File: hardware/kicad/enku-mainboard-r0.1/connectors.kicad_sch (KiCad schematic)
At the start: 4 parts

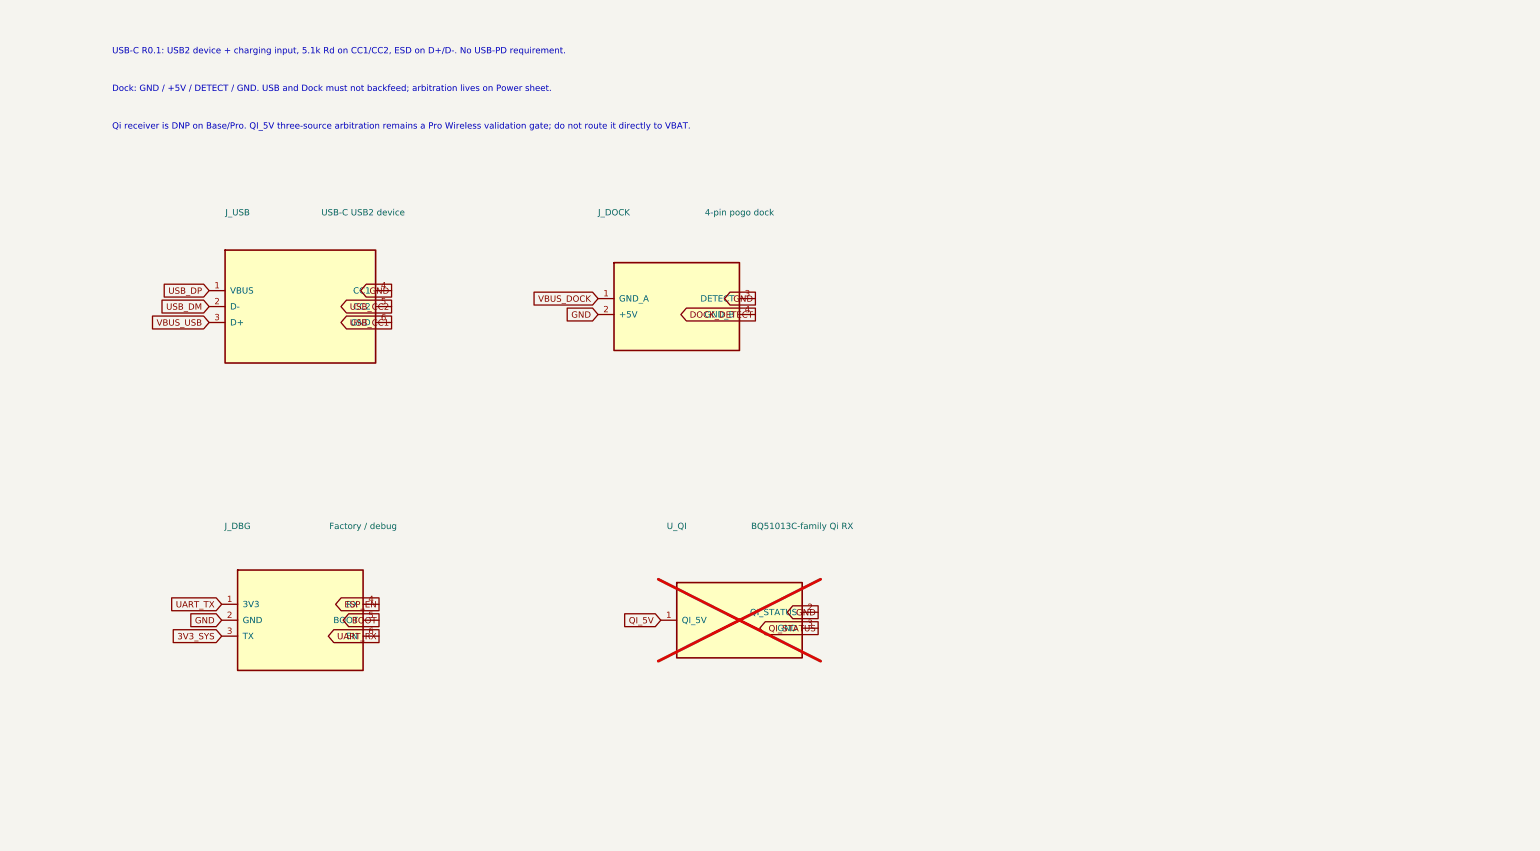
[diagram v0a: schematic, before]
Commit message: Expand USB-C and dock connector circuits
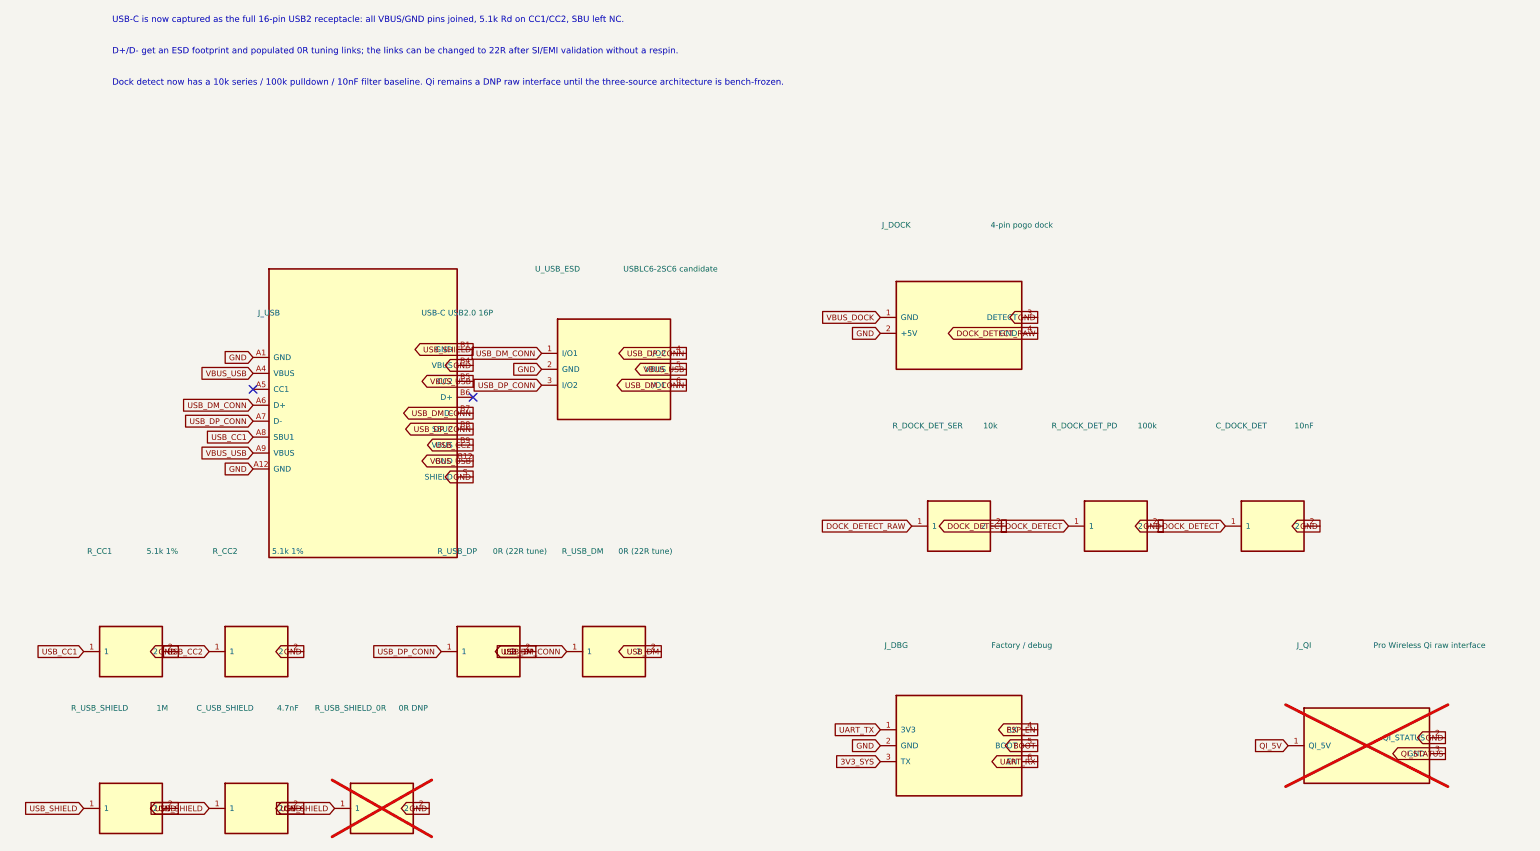
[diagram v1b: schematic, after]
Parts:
- removed J_DBG: Factory / debug, Connector_Generic:Conn_01x06, symbol ENKU:DEBUG_6P
- removed J_DOCK: 4-pin pogo dock, symbol ENKU:DOCK_4P
- removed J_USB: USB-C USB2 device, Connector_USB:USB_C_Receptacle_USB2.0_16P, symbol ENKU:USB_C_DEVICE
- removed U_QI: BQ51013C-family Qi RX, symbol ENKU:QI_RX_DNP
- added C_DOCK_DET: 10nF, Capacitor_SMD:C_0603_1608Metric, symbol ENKU:C
- added C_USB_SHIELD: 4.7nF, Capacitor_SMD:C_0603_1608Metric, symbol ENKU:C
- added J_DBG: Factory / debug, Connector_Generic:Conn_01x06, symbol ENKU:DEBUG6
- added J_DOCK: 4-pin pogo dock, ENKU:DOCK_POGO_4, symbol ENKU:DOCK4
- added J_QI: Pro Wireless Qi raw interface, Connector_Generic:Conn_01x03, symbol ENKU:QI3
- added J_USB: USB-C USB2.0 16P, Connector_USB:USB_C_Receptacle_USB2.0_16P, symbol ENKU:USB_C_16P
- added R_CC1, R_CC2: 5.1k 1%, Resistor_SMD:R_0603_1608Metric, symbol ENKU:R
- added R_DOCK_DET_PD: 100k, Resistor_SMD:R_0603_1608Metric, symbol ENKU:R
- added R_DOCK_DET_SER: 10k, Resistor_SMD:R_0603_1608Metric, symbol ENKU:R
- added R_USB_DM, R_USB_DP: 0R (22R tune), Resistor_SMD:R_0603_1608Metric, symbol ENKU:R
- added R_USB_SHIELD: 1M, Resistor_SMD:R_0603_1608Metric, symbol ENKU:R
- added R_USB_SHIELD_0R: 0R DNP, Resistor_SMD:R_0603_1608Metric, symbol ENKU:R
- added U_USB_ESD: USBLC6-2SC6 candidate, Package_TO_SOT_SMD:SOT-23-6, symbol ENKU:USB_ESD6
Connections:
- net 3V3_SYS: now also J_DBG.3 (TX)
- net BOOT: now also J_DBG.5 (BOOT)
- net DOCK_DETECT: now also C_DOCK_DET.1, R_DOCK_DET_PD.1, R_DOCK_DET_SER.2
- net ESP_EN: now also J_DBG.4 (RX)
- net GND: now also C_DOCK_DET.2, C_USB_SHIELD.2, J_DBG.2 (GND), J_DOCK.2 (+5V), J_DOCK.3 (DETECT), J_QI.2 (QI_STATUS), J_USB.A1 (GND), J_USB.A12 (GND), J_USB.B4 (VBUS), J_USB.S (SHIELD), R_CC1.2, R_CC2.2, R_DOCK_DET_PD.2, R_USB_SHIELD.2, R_USB_SHIELD_0R.2, U_USB_ESD.2 (GND)
- net QI_5V: now also J_QI.1 (QI_5V)
- net QI_STATUS: now also J_QI.3 (GND)
- net UART_RX: now also J_DBG.6 (EN)
- net UART_TX: now also J_DBG.1 (3V3)
- net USB_CC1: now also J_USB.A8 (SBU1), R_CC1.1
- net USB_CC2: now also J_USB.B9 (VBUS), R_CC2.1
- net USB_DM: now also R_USB_DM.2
- net USB_DP: now also R_USB_DP.2
- net VBUS_DOCK: now also J_DOCK.1 (GND)
- net VBUS_USB: now also J_USB.A4 (VBUS), J_USB.A9 (VBUS), J_USB.B12 (GND), J_USB.B5 (CC2), U_USB_ESD.5 (VBUS)
- new net DOCK_DETECT_RAW: J_DOCK.4 (GND), R_DOCK_DET_SER.1
- new net USB_DM_CONN: J_USB.A6 (D+), J_USB.B7 (D-), R_USB_DM.1, U_USB_ESD.1 (I/O1), U_USB_ESD.6 (I/O1)
- new net USB_DP_CONN: J_USB.A7 (D-), J_USB.B8 (SBU2), R_USB_DP.1, U_USB_ESD.3 (I/O2), U_USB_ESD.4 (I/O2)
- new net USB_SHIELD: C_USB_SHIELD.1, J_USB.B1 (GND), R_USB_SHIELD.1, R_USB_SHIELD_0R.1
- no-connect marks 0 -> 2
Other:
- note added: "D+/D- get an ESD footprint and populated 0R tuning links; the links can be changed to 22R after SI/EMI validation without a respin."
- note added: "Dock detect now has a 10k series / 100k pulldown / 10nF filter baseline. Qi remains a DNP raw interface until the three-source architecture is bench-frozen."
- note added: "USB-C is now captured as the full 16-pin USB2 receptacle: all VBUS/GND pins joined, 5.1k Rd on CC1/CC2, SBU left NC."
- note removed: "Dock: GND / +5V / DETECT / GND. USB and Dock must not backfeed; arbitration lives on Power sheet."
- note removed: "Qi receiver is DNP on Base/Pro. QI_5V three-source arbitration remains a Pro Wireless validation gate; do not route it directly to VBAT."
- note removed: "USB-C R0.1: USB2 device + charging input, 5.1k Rd on CC1/CC2, ESD on D+/D-. No USB-PD requirement."

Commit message: Freeze GCT USB4105-GF-A-120 in R0.1 schematic
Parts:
- J_USB: value USB-C USB2.0 16P -> GCT USB4105-GF-A-120; footprint Connector_USB:USB_C_Receptacle_USB2.0_16P -> Connector_USB:USB_C_Receptacle_GCT_USB4105-xx-A_16P_TopMnt_Horizontal
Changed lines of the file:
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@@
 	(symbol (lib_id "ENKU:USB_C_16P") (at 65 82 0) (unit 1) (exclude_from_sim no) (in_bom yes) (on_board yes) (dnp no)
 		(property "Reference" "J_USB" (at 50 66 0) (effects (font (size 0.9 0.9))))
-		(property "Value" "USB-C USB2.0 16P" (at 80 66 0) (effects (font (size 0.9 0.9))))
-		(property "Footprint" "Connector_USB:USB_C_Receptacle_USB2.0_16P" (at 65 82 0) (effects (font (size 0.9 0.9)) (hide yes)))
+		(property "Value" "GCT USB4105-GF-A-120" (at 80 66 0) (effects (font (size 0.9 0.9))))
+		(property "Footprint" "Connector_USB:USB_C_Receptacle_GCT_USB4105-xx-A_16P_TopMnt_Horizontal" (at 65 82 0) (effects (font (size 0.9 0.9)) (hide yes)))
 		(property "Datasheet" "~" (at 65 82 0) (effects (font (size 0.9 0.9)) (hide yes)))
-		(property "Description" "USB-C USB2.0 16P" (at 65 82 0) (effects (font (size 0.9 0.9)) (hide yes)))
+		(property "Description" "GCT USB4105-GF-A-120" (at 65 82 0) (effects (font (size 0.9 0.9)) (hide yes)))
 		(pin "A1")
 		(pin "A4")

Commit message: Freeze USB ESD and use virtual factory debug footprint
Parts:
- J_DBG: value Factory / debug -> Tag-Connect TC2030-IDC-NL; footprint Connector_Generic:Conn_01x06 -> Connector:Tag-Connect_TC2030-IDC-NL_2x03_P1.27mm_Vertical; now left out of the parts list
- J_QI: value Pro Wireless Qi raw interface -> Pro Wireless Qi raw interface — DNP; footprint Connector_Generic:Conn_01x03 -> ENKU:QI_RAW_3
- U_USB_ESD: value USBLC6-2SC6 candidate -> USBLC6-2SC6
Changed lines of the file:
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@@
 	(symbol (lib_id "ENKU:USB_ESD6") (at 105 75 0) (unit 1) (exclude_from_sim no) (in_bom yes) (on_board yes) (dnp no)
 		(property "Reference" "U_USB_ESD" (at 96 59 0) (effects (font (size 0.9 0.9))))
-		(property "Value" "USBLC6-2SC6 candidate" (at 114 59 0) (effects (font (size 0.9 0.9))))
+		(property "Value" "USBLC6-2SC6" (at 114 59 0) (effects (font (size 0.9 0.9))))
 		(property "Footprint" "Package_TO_SOT_SMD:SOT-23-6" (at 105 75 0) (effects (font (size 0.9 0.9)) (hide yes)))
 		(property "Datasheet" "~" (at 105 75 0) (effects (font (size 0.9 0.9)) (hide yes)))
-		(property "Description" "USBLC6-2SC6 candidate" (at 105 75 0) (effects (font (size 0.9 0.9)) (hide yes)))
+		(property "Description" "USBLC6-2SC6" (at 105 75 0) (effects (font (size 0.9 0.9)) (hide yes)))
 		(pin "1")
 		(pin "2")
@@
 	(global_label "DOCK_DETECT" (shape input) (at 202.46 100 0) (effects (font (size 0.9 0.9)) (justify right bottom)))
 	(global_label "GND" (shape output) (at 217.54 100 180) (effects (font (size 0.9 0.9)) (justify right bottom)))
-	(symbol (lib_id "ENKU:DEBUG6") (at 160 135 0) (unit 1) (exclude_from_sim no) (in_bom yes) (on_board yes) (dnp no)
+	(symbol (lib_id "ENKU:DEBUG6") (at 160 135 0) (unit 1) (exclude_from_sim no) (in_bom no) (on_board yes) (dnp no)
 		(property "Reference" "J_DBG" (at 150 119 0) (effects (font (size 0.9 0.9))))
-		(property "Value" "Factory / debug" (at 170 119 0) (effects (font (size 0.9 0.9))))
-		(property "Footprint" "Connector_Generic:Conn_01x06" (at 160 135 0) (effects (font (size 0.9 0.9)) (hide yes)))
+		(property "Value" "Tag-Connect TC2030-IDC-NL" (at 170 119 0) (effects (font (size 0.9 0.9))))
+		(property "Footprint" "Connector:Tag-Connect_TC2030-IDC-NL_2x03_P1.27mm_Vertical" (at 160 135 0) (effects (font (size 0.9 0.9)) (hide yes)))
 		(property "Datasheet" "~" (at 160 135 0) (effects (font (size 0.9 0.9)) (hide yes)))
 		(property "Description" "Factory / debug" (at 160 135 0) (effects (font (size 0.9 0.9)) (hide yes)))
@@
 	(symbol (lib_id "ENKU:QI3") (at 225 135 0) (unit 1) (exclude_from_sim no) (in_bom yes) (on_board yes) (dnp yes)
 		(property "Reference" "J_QI" (at 215 119 0) (effects (font (size 0.9 0.9))))
-		(property "Value" "Pro Wireless Qi raw interface" (at 235 119 0) (effects (font (size 0.9 0.9))))
-		(property "Footprint" "Connector_Generic:Conn_01x03" (at 225 135 0) (effects (font (size 0.9 0.9)) (hide yes)))
+		(property "Value" "Pro Wireless Qi raw interface — DNP" (at 235 119 0) (effects (font (size 0.9 0.9))))
+		(property "Footprint" "ENKU:QI_RAW_3" (at 225 135 0) (effects (font (size 0.9 0.9)) (hide yes)))
 		(property "Datasheet" "~" (at 225 135 0) (effects (font (size 0.9 0.9)) (hide yes)))
 		(property "Description" "Pro Wireless Qi raw interface" (at 225 135 0) (effects (font (size 0.9 0.9)) (hide yes)))
